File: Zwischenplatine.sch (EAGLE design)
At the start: 7 parts

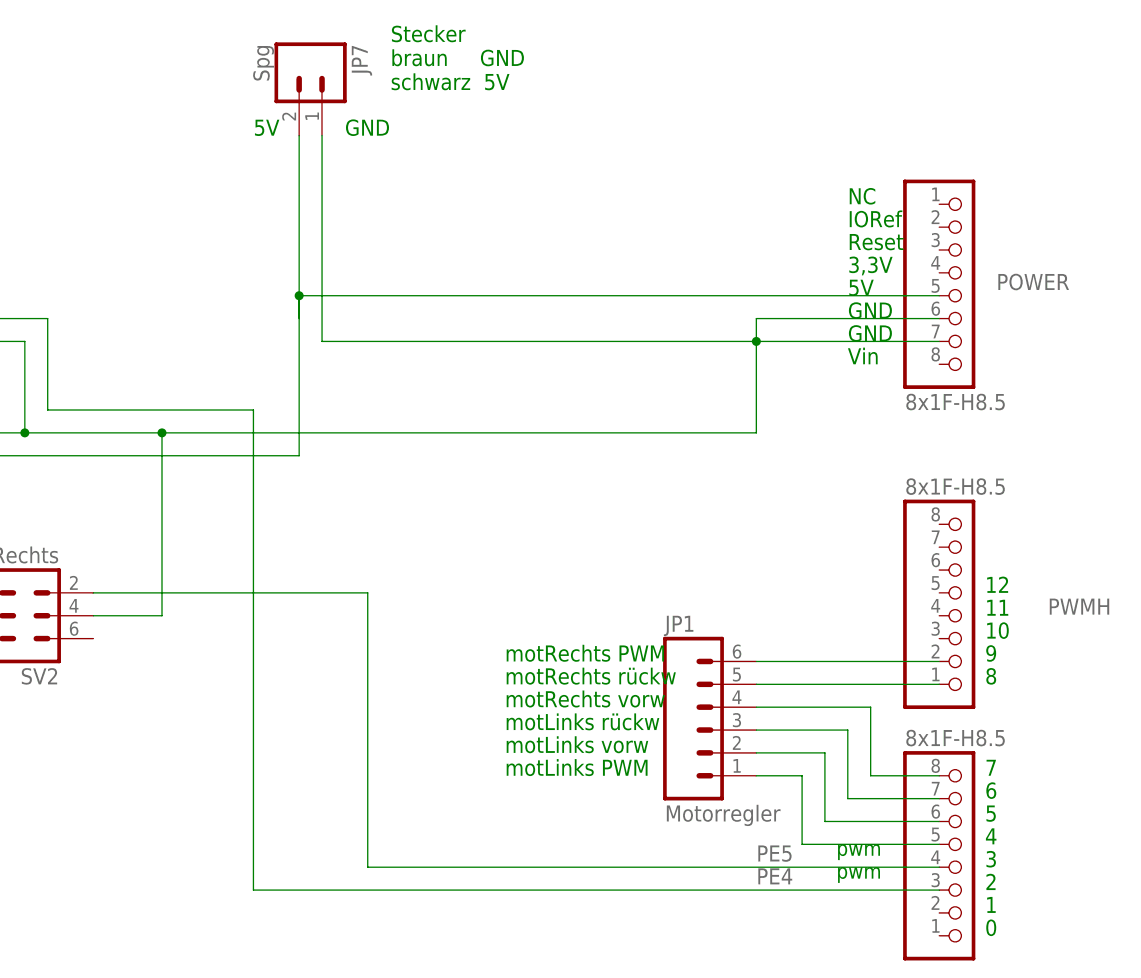
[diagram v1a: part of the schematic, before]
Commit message: 
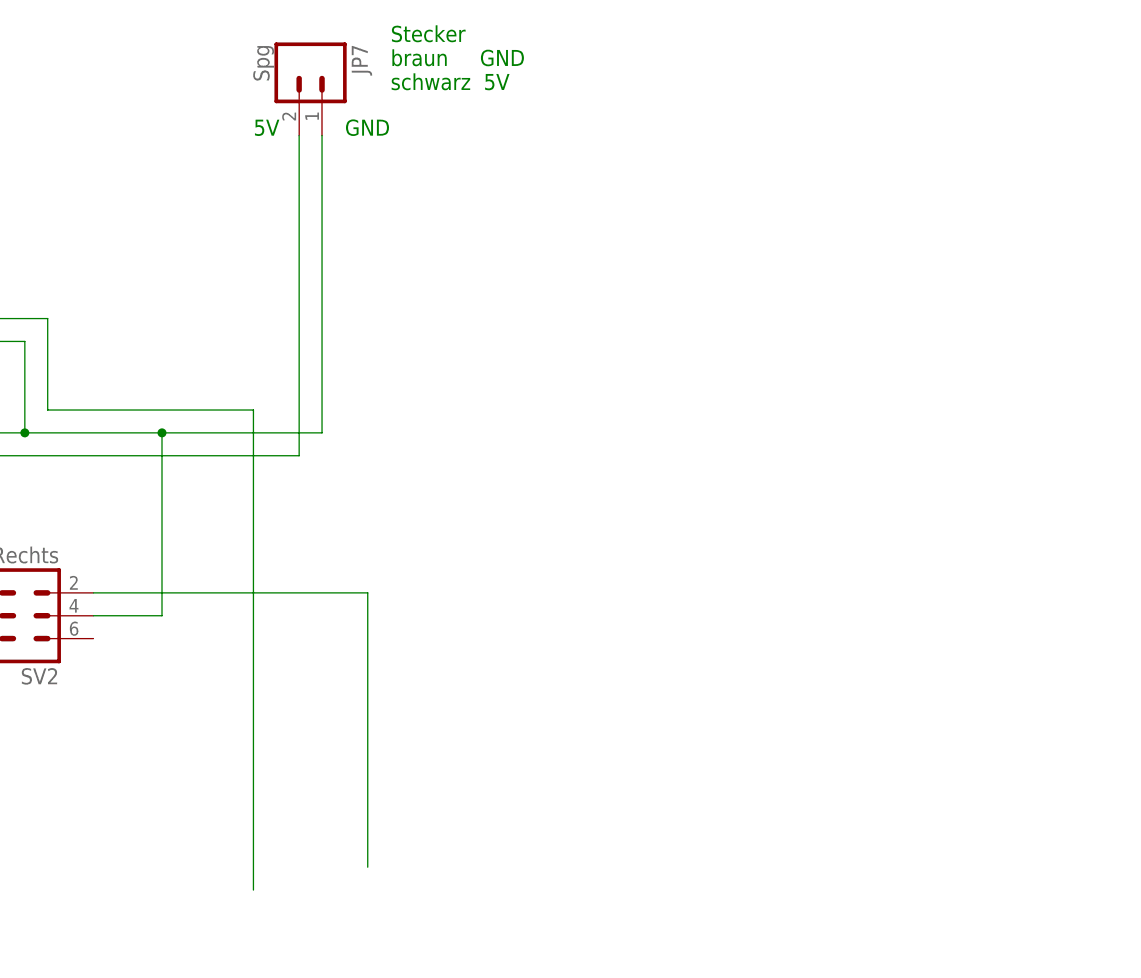
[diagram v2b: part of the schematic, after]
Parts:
- removed JP1: Motorregler, SparkFun-Connectors:M06LOCK
- removed POWER, PWMH, PWML: 8x1F-H8.5, SmartPrj:PINHD-1X8
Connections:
- removed net N$16: JP1.4, PWML.8
- removed net N$17: JP1.3, PWML.7
- removed net N$18: JP1.2, PWML.6
- removed net N$19: JP1.1, PWML.5
- removed net N$3: JP1.6, PWMH.2
- removed net N$4: JP1.5, PWMH.1
- net N$1: no longer POWER.5
- net N$2: no longer POWER.6, POWER.7
- net PE4: no longer PWML.3
- net PE5: no longer PWML.4
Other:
- note removed: "0"
- note removed: "1"
- note removed: "10"
- note removed: "11"
- note removed: "12"
- note removed: "2"
- note removed: "3"
- note removed: "3,3V"
- note removed: "4"
- note removed: "5"
- note removed: "6"
- note removed: "7"
- note removed: "8"
- note removed: "9"
- note removed: "IORef"
- note removed: "NC"
- note removed: "Reset"
- note removed: "Vin"
- note removed: "motLinks PWM"
- note removed: "motLinks rückw"
- note removed: "motLinks vorw"
- note removed: "motRechts PWM"
- note removed: "motRechts rückw"
- note removed: "motRechts vorw"
- note removed: "pwm"
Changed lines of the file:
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@@
 <part name="SV2" library="con-ml" deviceset="ML6" device="" value="Encoder_Rechts"/>
 <part name="JP7" library="SparkFun-Connectors" deviceset="M02" device="-JST-2MM-SMT" value="Spg"/>
-<part name="PWML" library="SmartPrj" deviceset="PINHD-1X8" device="" value="8x1F-H8.5"/>
-<part name="POWER" library="SmartPrj" deviceset="PINHD-1X8" device="" value="8x1F-H8.5"/>
-<part name="PWMH" library="SmartPrj" deviceset="PINHD-1X8" device="" value="8x1F-H8.5"/>
-<part name="JP1" library="SparkFun-Connectors" deviceset="M06" device="LOCK" value="Motorregler"/>
 </parts>
 <sheets>
 <sheet>
 <plain>
-<text x="134.62" y="50.8" size="1.778" layer="91">0</text>
-<text x="134.62" y="53.34" size="1.778" layer="91">1</text>
-<text x="134.62" y="55.88" size="1.778" layer="91">2</text>
-<text x="134.62" y="58.42" size="1.778" layer="91">3</text>
-<text x="134.62" y="60.96" size="1.778" layer="91">4</text>
-<text x="134.62" y="63.5" size="1.778" layer="91">5</text>
-<text x="134.62" y="66.04" size="1.778" layer="91">6</text>
-<text x="134.62" y="68.58" size="1.778" layer="91">7</text>
-<text x="118.11" y="57.15" size="1.6764" layer="91">pwm</text>
-<text x="118.11" y="59.69" size="1.6764" layer="91">pwm</text>
-<text x="119.38" y="121.92" size="1.778" layer="91">5V</text>
-<text x="119.38" y="119.38" size="1.778" layer="91">GND</text>
-<text x="119.38" y="116.84" size="1.778" layer="91">GND</text>
 <text x="63.5" y="139.7" size="1.778" layer="91">GND</text>
 <text x="53.34" y="139.7" size="1.778" layer="91">5V</text>
-<text x="119.38" y="114.3" size="1.778" layer="91">Vin</text>
-<text x="119.38" y="124.46" size="1.778" layer="91">3,3V</text>
-<text x="119.38" y="127" size="1.778" layer="91">Reset</text>
-<text x="119.38" y="129.54" size="1.778" layer="91">IORef</text>
-<text x="119.38" y="132.08" size="1.778" layer="91">NC</text>
-<text x="134.62" y="78.74" size="1.778" layer="91">8</text>
-<text x="134.62" y="81.28" size="1.778" layer="91">9</text>
-<text x="134.62" y="83.82" size="1.778" layer="91">10</text>
-<text x="134.62" y="86.36" size="1.778" layer="91">11</text>
-<text x="134.62" y="88.9" size="1.778" layer="91">12</text>
-<text x="81.28" y="68.58" size="1.778" layer="91">motLinks PWM</text>
-<text x="81.28" y="71.12" size="1.778" layer="91">motLinks vorw</text>
-<text x="81.28" y="73.66" size="1.778" layer="91">motLinks rückw</text>
-<text x="81.28" y="76.2" size="1.778" layer="91">motRechts vorw</text>
-<text x="81.28" y="78.74" size="1.778" layer="91">motRechts rückw</text>
-<text x="81.28" y="81.28" size="1.778" layer="91">motRechts PWM</text>
 <text x="68.58" y="144.78" size="1.778" layer="91">Stecker
 braun     GND
@@
 </instance>
 <instance part="JP7" gate="G$1" x="58.42" y="147.32" rot="R270"/>
-<instance part="PWML" gate="A" x="132.08" y="60.96" smashed="yes" rot="MR180">
-<attribute name="VALUE" x="125.73" y="73.66" size="1.778" layer="96" rot="MR180"/>
-</instance>
-<instance part="POWER" gate="A" x="132.08" y="121.92" smashed="yes">
-<attribute name="NAME" x="135.89" y="122.555" size="1.778" layer="95"/>
-<attribute name="VALUE" x="125.73" y="109.22" size="1.778" layer="96"/>
-</instance>
-<instance part="PWMH" gate="A" x="132.08" y="88.9" smashed="yes" rot="MR180">
-<attribute name="NAME" x="141.605" y="88.265" size="1.778" layer="95" rot="MR180"/>
-<attribute name="VALUE" x="125.73" y="101.6" size="1.778" layer="96" rot="MR180"/>
-</instance>
-<instance part="JP1" gate="G$1" x="104.14" y="73.66"/>
 </instances>
 <busses>
@@
 <wire x1="35.56" y1="88.9" x2="66.04" y2="88.9" width="0.1524" layer="91"/>
 <wire x1="66.04" y1="88.9" x2="66.04" y2="58.42" width="0.1524" layer="91"/>
-<wire x1="66.04" y1="58.42" x2="129.54" y2="58.42" width="0.1524" layer="91"/>
-<label x="109.22" y="59.055" size="1.778" layer="95"/>
-<pinref part="PWML" gate="A" pin="4"/>
 <pinref part="SV2" gate="1" pin="2"/>
 </segment>
@@
 <net name="PE4" class="0">
 <segment>
-<wire x1="53.34" y1="55.88" x2="129.54" y2="55.88" width="0.1524" layer="91"/>
-<label x="109.22" y="56.515" size="1.778" layer="95"/>
-<pinref part="PWML" gate="A" pin="3"/>
 <wire x1="30.48" y1="119.38" x2="30.48" y2="109.22" width="0.1524" layer="91"/>
 <wire x1="30.48" y1="109.22" x2="53.34" y2="109.22" width="0.1524" layer="91"/>
@@
 <net name="N$1" class="3">
 <segment>
-<wire x1="58.42" y1="104.14" x2="58.42" y2="121.92" width="0.1524" layer="91"/>
-<wire x1="58.42" y1="121.92" x2="58.42" y2="139.7" width="0.1524" layer="91"/>
+<wire x1="58.42" y1="104.14" x2="58.42" y2="139.7" width="0.1524" layer="91"/>
 <wire x1="5.08" y1="114.3" x2="5.08" y2="104.14" width="0.1524" layer="91"/>
 <wire x1="5.08" y1="104.14" x2="5.08" y2="83.82" width="0.1524" layer="91"/>
@@
 <junction x="5.08" y="104.14"/>
 <pinref part="JP7" gate="G$1" pin="1"/>
-<pinref part="POWER" gate="A" pin="5"/>
-<wire x1="129.54" y1="121.92" x2="58.42" y2="121.92" width="0.1524" layer="91"/>
-<wire x1="58.42" y1="121.92" x2="58.42" y2="119.38" width="0.1524" layer="91"/>
-<junction x="58.42" y="121.92"/>
 <pinref part="SV1" gate="1" pin="5"/>
 <wire x1="7.62" y1="114.3" x2="5.08" y2="114.3" width="0.1524" layer="91"/>
@@
 <net name="N$2" class="2">
 <segment>
-<wire x1="129.54" y1="119.38" x2="109.22" y2="119.38" width="0.1524" layer="91"/>
-<wire x1="109.22" y1="119.38" x2="109.22" y2="116.84" width="0.1524" layer="91"/>
-<wire x1="129.54" y1="116.84" x2="109.22" y2="116.84" width="0.1524" layer="91"/>
-<junction x="109.22" y="116.84"/>
-<pinref part="POWER" gate="A" pin="6"/>
-<pinref part="POWER" gate="A" pin="7"/>
-<wire x1="60.96" y1="139.7" x2="60.96" y2="116.84" width="0.1524" layer="91"/>
-<wire x1="60.96" y1="116.84" x2="109.22" y2="116.84" width="0.1524" layer="91"/>
+<wire x1="60.96" y1="139.7" x2="60.96" y2="106.68" width="0.1524" layer="91"/>
 <pinref part="SV1" gate="1" pin="3"/>
 <wire x1="7.62" y1="116.84" x2="2.54" y2="116.84" width="0.1524" layer="91"/>
@@
 <wire x1="2.54" y1="106.68" x2="27.94" y2="106.68" width="0.1524" layer="91"/>
 <wire x1="27.94" y1="106.68" x2="43.18" y2="106.68" width="0.1524" layer="91"/>
-<wire x1="43.18" y1="106.68" x2="109.22" y2="106.68" width="0.1524" layer="91"/>
-<wire x1="109.22" y1="106.68" x2="109.22" y2="116.84" width="0.1524" layer="91"/>
+<wire x1="43.18" y1="106.68" x2="60.96" y2="106.68" width="0.1524" layer="91"/>
 <wire x1="27.94" y1="116.84" x2="27.94" y2="106.68" width="0.1524" layer="91"/>
 <wire x1="2.54" y1="106.68" x2="2.54" y2="86.36" width="0.1524" layer="91"/>
@@
 </segment>
 </net>
-<net name="N$16" class="0">
-<segment>
-<pinref part="PWML" gate="A" pin="8"/>
-<wire x1="129.54" y1="68.58" x2="121.92" y2="68.58" width="0.1524" layer="91"/>
-<wire x1="121.92" y1="68.58" x2="121.92" y2="76.2" width="0.1524" layer="91"/>
-<pinref part="JP1" gate="G$1" pin="4"/>
-<wire x1="121.92" y1="76.2" x2="109.22" y2="76.2" width="0.1524" layer="91"/>
-</segment>
-</net>
-<net name="N$17" class="0">
-<segment>
-<pinref part="PWML" gate="A" pin="7"/>
-<wire x1="129.54" y1="66.04" x2="119.38" y2="66.04" width="0.1524" layer="91"/>
-<wire x1="119.38" y1="66.04" x2="119.38" y2="73.66" width="0.1524" layer="91"/>
-<pinref part="JP1" gate="G$1" pin="3"/>
-<wire x1="119.38" y1="73.66" x2="109.22" y2="73.66" width="0.1524" layer="91"/>
-</segment>
-</net>
-<net name="N$18" class="0">
-<segment>
-<pinref part="PWML" gate="A" pin="6"/>
-<wire x1="129.54" y1="63.5" x2="116.84" y2="63.5" width="0.1524" layer="91"/>
-<wire x1="116.84" y1="63.5" x2="116.84" y2="71.12" width="0.1524" layer="91"/>
-<pinref part="JP1" gate="G$1" pin="2"/>
-<wire x1="109.22" y1="71.12" x2="116.84" y2="71.12" width="0.1524" layer="91"/>
-</segment>
-</net>
-<net name="N$19" class="0">
-<segment>
-<pinref part="PWML" gate="A" pin="5"/>
-<wire x1="129.54" y1="60.96" x2="114.3" y2="60.96" width="0.1524" layer="91"/>
-<wire x1="114.3" y1="60.96" x2="114.3" y2="68.58" width="0.1524" layer="91"/>
-<pinref part="JP1" gate="G$1" pin="1"/>
-<wire x1="109.22" y1="68.58" x2="114.3" y2="68.58" width="0.1524" layer="91"/>
-</segment>
-</net>
-<net name="N$3" class="0">
-<segment>
-<pinref part="JP1" gate="G$1" pin="6"/>
-<pinref part="PWMH" gate="A" pin="2"/>
-<wire x1="109.22" y1="81.28" x2="129.54" y2="81.28" width="0.1524" layer="91"/>
-</segment>
-</net>
-<net name="N$4" class="0">
-<segment>
-<pinref part="JP1" gate="G$1" pin="5"/>
-<pinref part="PWMH" gate="A" pin="1"/>
-<wire x1="109.22" y1="78.74" x2="129.54" y2="78.74" width="0.1524" layer="91"/>
-</segment>
-</net>

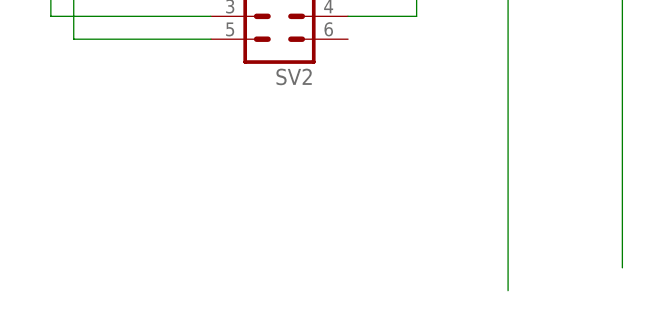
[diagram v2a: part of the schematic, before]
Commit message: 
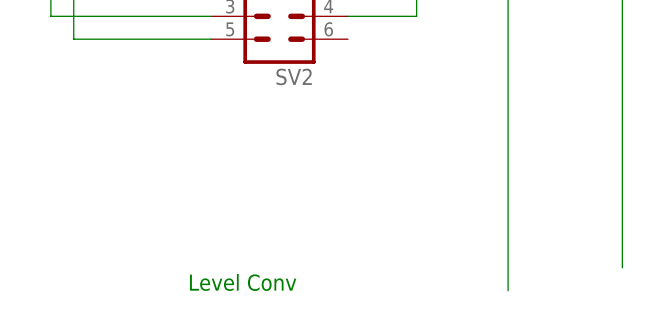
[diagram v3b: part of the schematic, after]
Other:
- note added: "Level Conv"
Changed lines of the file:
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@@
 braun     GND
 schwarz  5V</text>
+<text x="17.78" y="55.88" size="1.778" layer="91">Level Conv</text>
 </plain>
 <instances>
